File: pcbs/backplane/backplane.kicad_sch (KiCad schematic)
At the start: 101 parts, among them J1 Conn_01x02, J10 AFBR-2624Z, J11 AFBR-2624Z, J12 AFBR-1624Z, J14 Conn_01x02, J17 Conn_01x02, J19 Conn_01x02, J22 Conn_01x02, J24 Conn_01x02, J27 Conn_01x02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

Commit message: Finished migrating footprint names
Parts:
- TP1, TP2, TP3, TP5: footprint TestPoint:TestPoint_Keystone_5019_Minature -> TestPoint:TestPoint_Keystone_5019_Miniature
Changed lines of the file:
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@@
 			)
 		)
-		(property "Footprint" "TestPoint:TestPoint_Keystone_5019_Minature"
+		(property "Footprint" "TestPoint:TestPoint_Keystone_5019_Miniature"
 			(at 46.99 274.32 0)
 			(effects
@@
 			)
 		)
-		(property "Footprint" "TestPoint:TestPoint_Keystone_5019_Minature"
+		(property "Footprint" "TestPoint:TestPoint_Keystone_5019_Miniature"
 			(at 33.02 55.88 0)
 			(effects
@@
 			)
 		)
-		(property "Footprint" "TestPoint:TestPoint_Keystone_5019_Minature"
+		(property "Footprint" "TestPoint:TestPoint_Keystone_5019_Miniature"
 			(at 33.02 62.23 0)
 			(effects
@@
 			)
 		)
-		(property "Footprint" "TestPoint:TestPoint_Keystone_5019_Minature"
+		(property "Footprint" "TestPoint:TestPoint_Keystone_5019_Miniature"
 			(at 184.15 26.67 0)
 			(effects

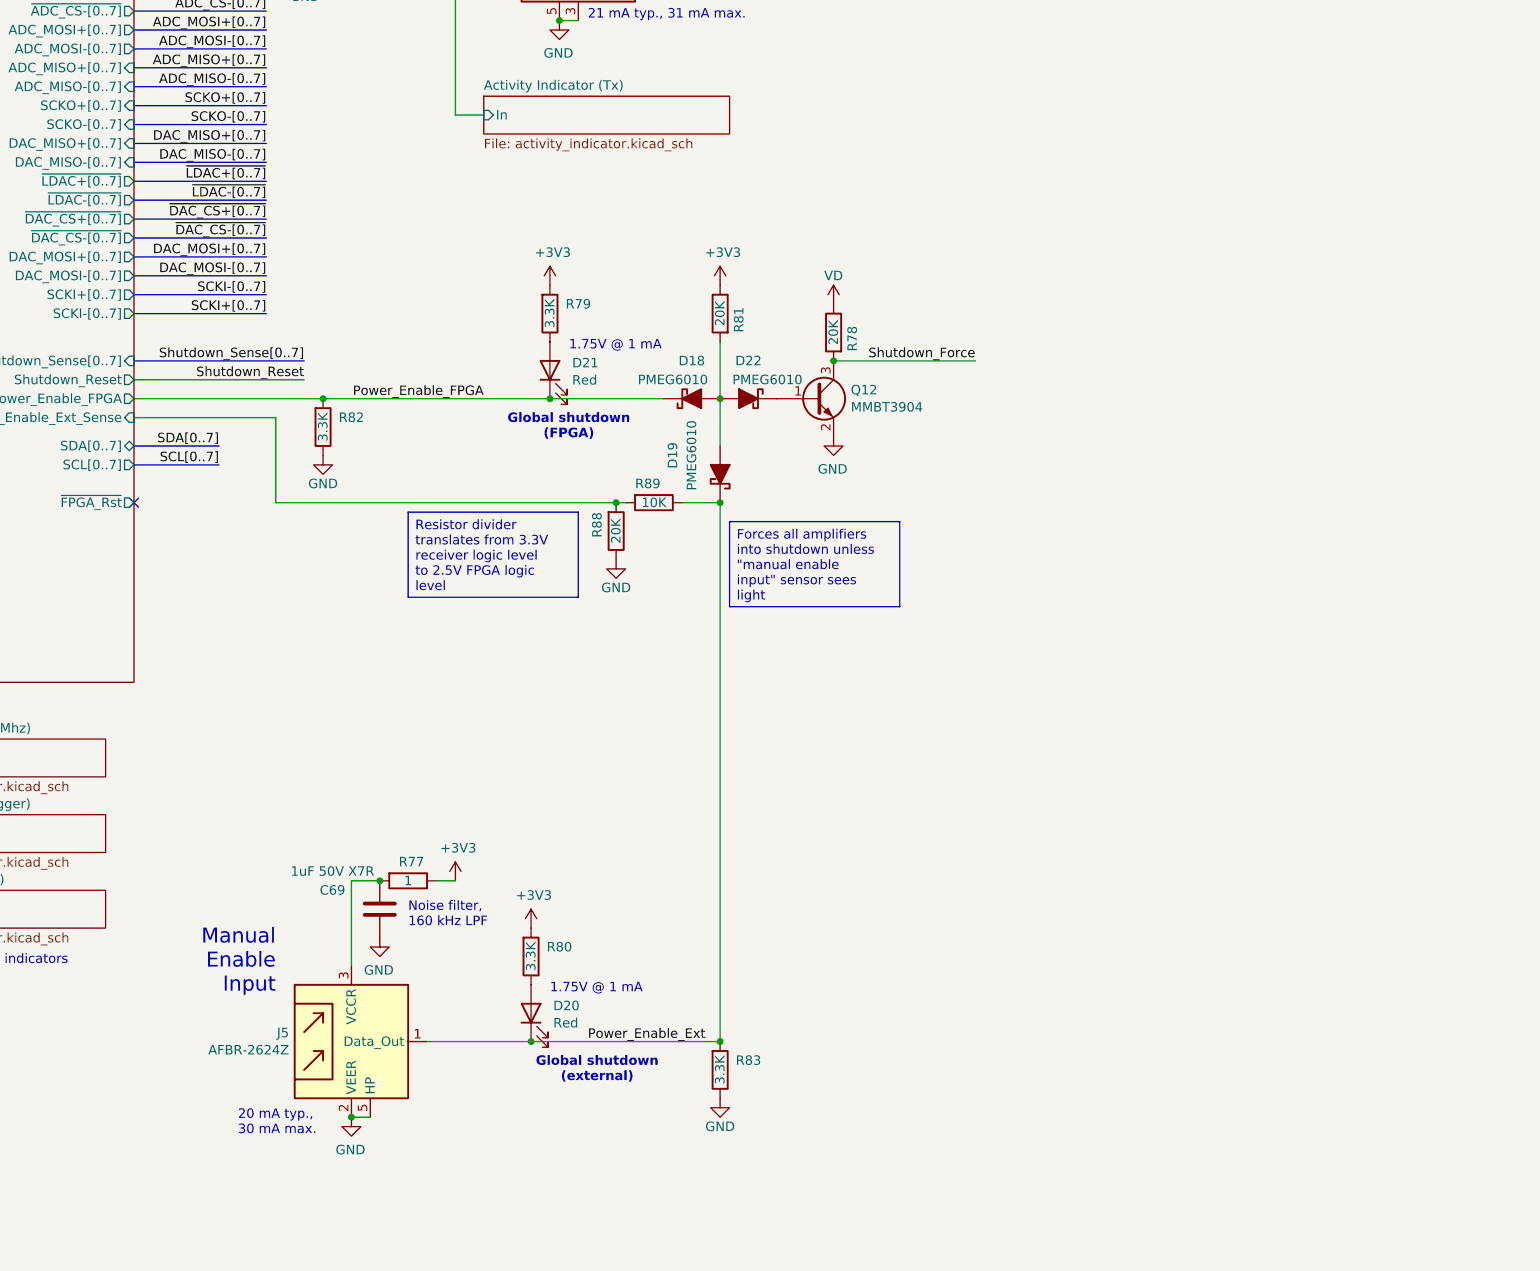
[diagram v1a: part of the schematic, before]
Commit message: BOM & reset fixes
Amp ctrl: changed name of "Manufacturer" field to "MPN" to work with Aisler
Amp ctrl: added part number to logic inverter, corrected various typos and part number problems
Backplane: added pull-down to Shutdown_Reset signal (#35)
Backplane: rethought Shutdown_Force circuit to make fail-safe (broken connections->shutdown), make work correctly (fixes #35)
Backplane: updated/corrected various schematic annotations
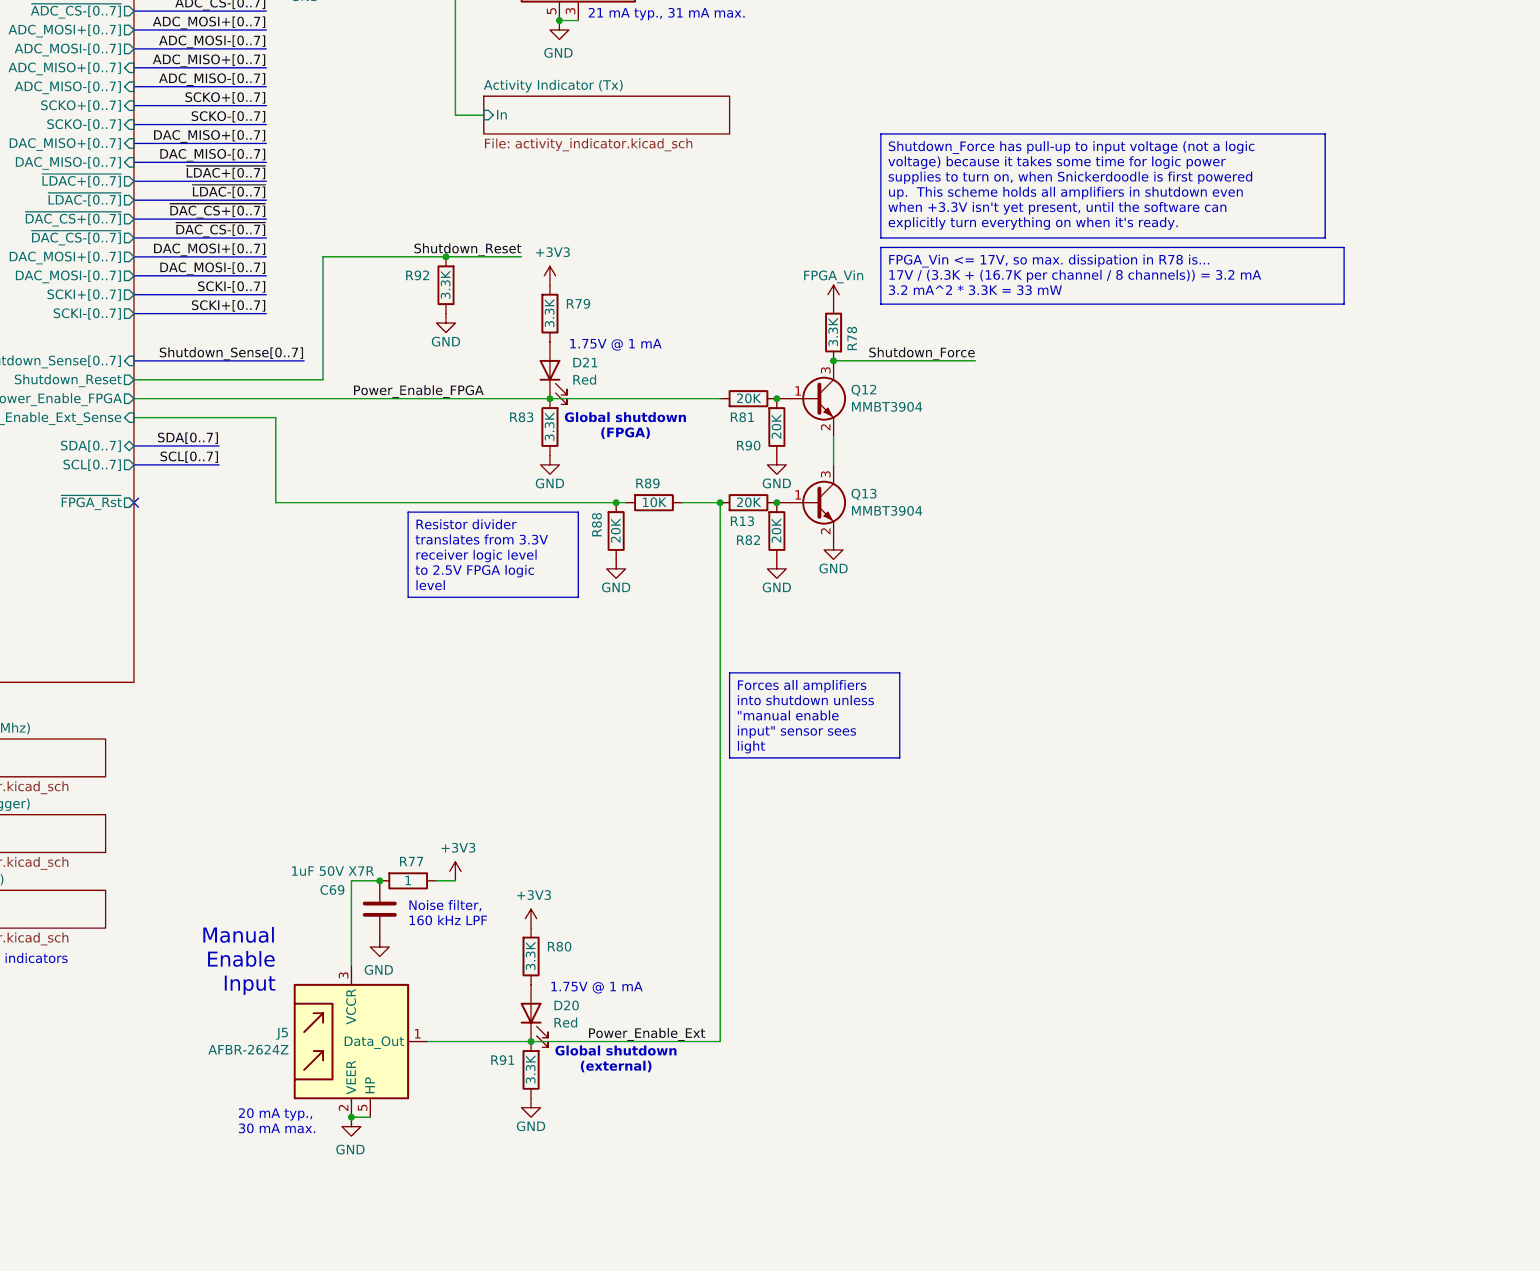
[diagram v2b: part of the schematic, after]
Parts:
- removed D18, D19, D22: PMEG6010, Diode_SMD:D_SOD-123F, symbol backplane-rescue:D_Schottky_ALT-Device
- added Q13: MMBT3904, Package_TO_SOT_SMD:SOT-23, symbol Transistor_BJT:MMBT3904
- added R13, R90: 20K, Resistor_SMD:R_0805_2012Metric, symbol Device:R
- added R91, R92: 3.3K, Resistor_SMD:R_0805_2012Metric, symbol Device:R
- R78: value 20K -> 3.3K; Part Number RK73H2ATTD2002F -> RK73H2ATTD3301F
- R82: value 3.3K -> 20K; Part Number RK73H2ATTD3301F -> RK73H2ATTD2002F
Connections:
- net +3V3: no longer R81.1
- net GND: now also Q13.2 (E), R90.1, R91.1, R92.1; no longer Q12.2 (E)
- net Power_Enable_Ext: now also R13.2, R91.2; no longer R83.2
- net Power_Enable_FPGA: now also R81.2, R83.2; no longer R82.2
- net Shutdown_Reset: now also R92.2
- net VD: no longer R78.1
- net at Q12.1 (B): now also R81.1, R90.2
- new net: Q13.1 (B), R13.1, R82.2
- new net: Q12.2 (E), Q13.3 (C)
- new net FPGA_Vin: R78.1
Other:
- moved on the sheet: R81, R82
